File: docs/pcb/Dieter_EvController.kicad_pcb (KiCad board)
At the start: 2 copper layers, 60 x 93.5 mm, 37 parts, among them IC1 ADS1118QDGSRQ1, J1 HVDC_POS, J2 HVDC_NEG, J6 lock_motor, J7 inputs, J8 relay board, J9 PLC_modem, Q1 set state c, U6 ISOW7741

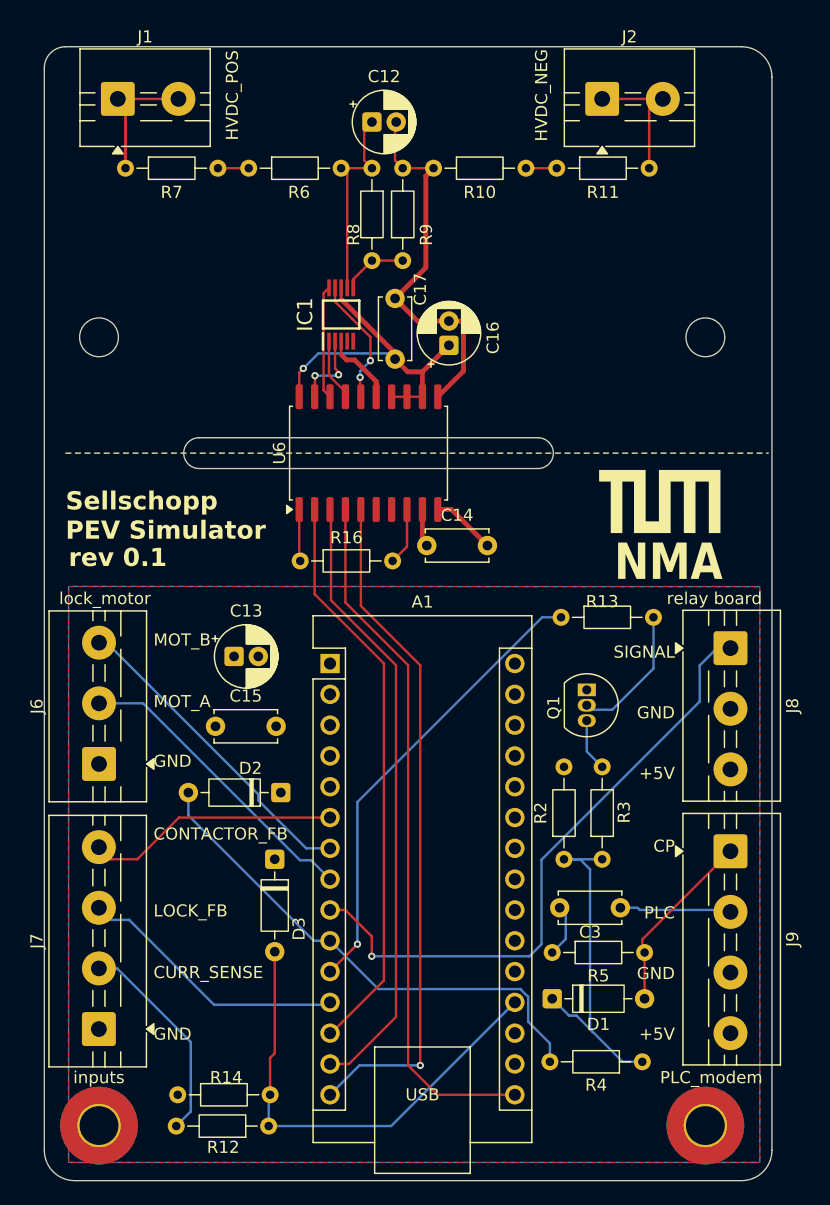
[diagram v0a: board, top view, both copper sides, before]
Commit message: documentation: add mounting + corrected pcb source files; BOM
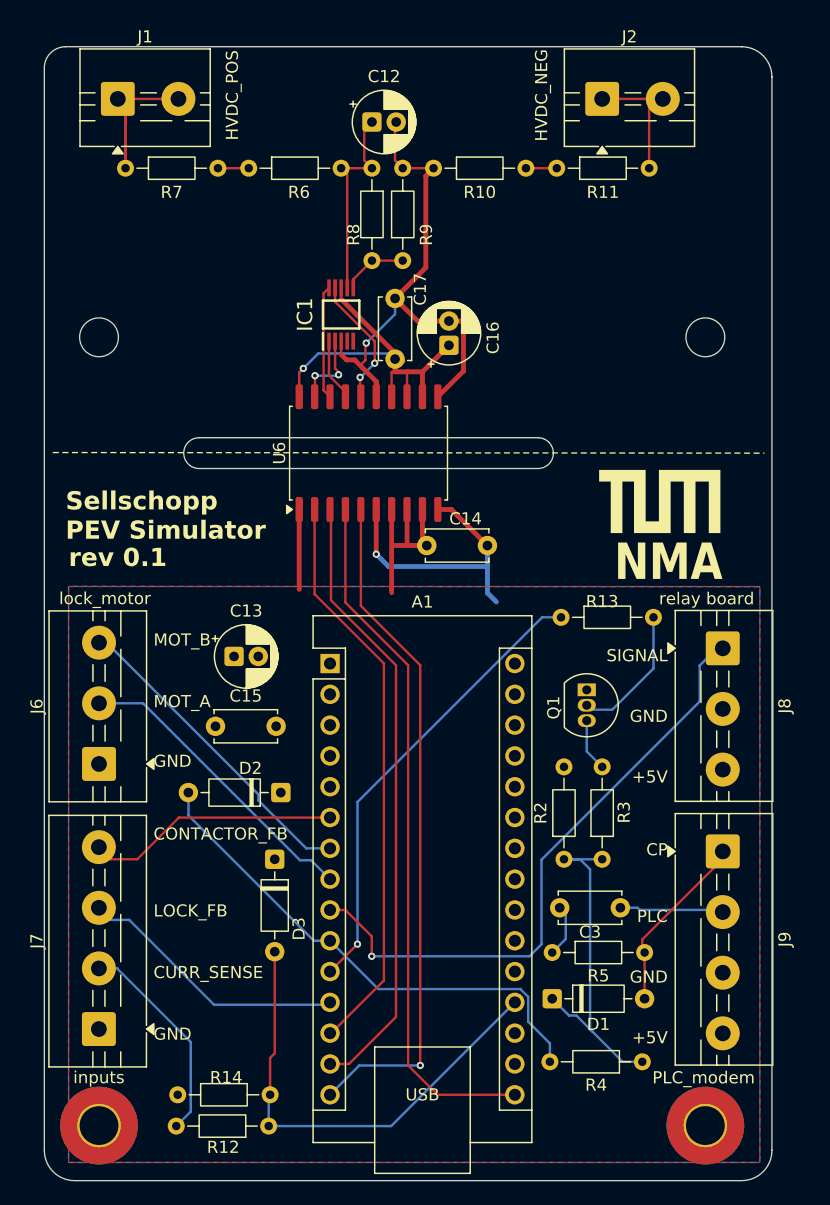
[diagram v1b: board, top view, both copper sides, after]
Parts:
- removed R16: 10k, Resistor_THT:R_Axial_DIN0204_L3.6mm_D1.6mm_P7.62mm_Horizontal
- Q1: value set state c -> 2N7000
- moved J8 0.64 mm to (67.9, 148.6)
- moved J9 0.64 mm to (67.9, 165.4)
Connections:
- U6 pad 8: Net-(U6-EN/FLT) -> +5C
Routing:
- net GND: track 5.32 -> 23.6 mm, vias 0 -> 1
- net +5C: track 7.67 -> 23.8 mm
- net ISO_ADC_GND: track 39.3 -> 45.2 mm, vias 0 -> 1
- net Net-(U6-EN/FLT): track 4.73 -> 0.00 mm
- net ISO_ADC_+5V: track 30.2 -> 32.7 mm
- net /POWER_RELAY: track 51.9 -> 51.3 mm
- net /PLC_MODEM: track 9.22 -> 8.59 mm
